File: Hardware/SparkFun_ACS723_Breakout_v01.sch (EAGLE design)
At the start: 13 parts

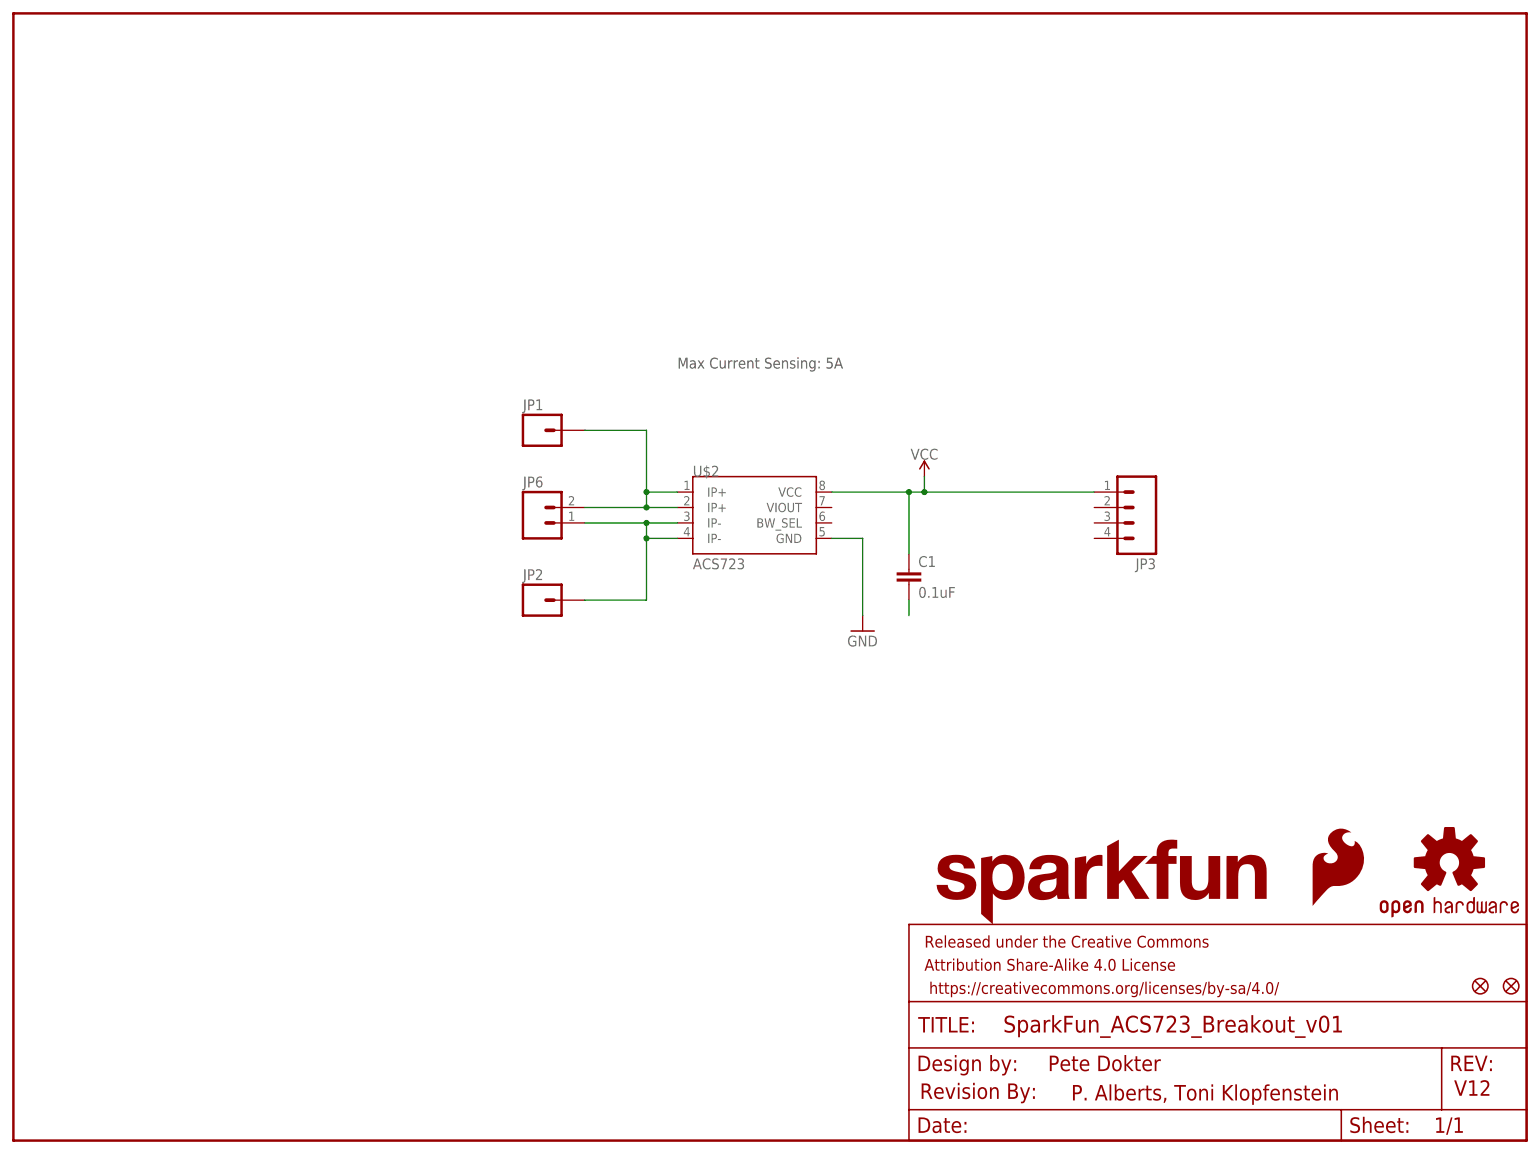
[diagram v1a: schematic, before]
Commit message: Finalizing v01 hardware
-Adjusted silk
-Isolated high current side of the board
-added recommended filter caps
-added band-width select jumper
-changed version number
-changed chip package to ACS723
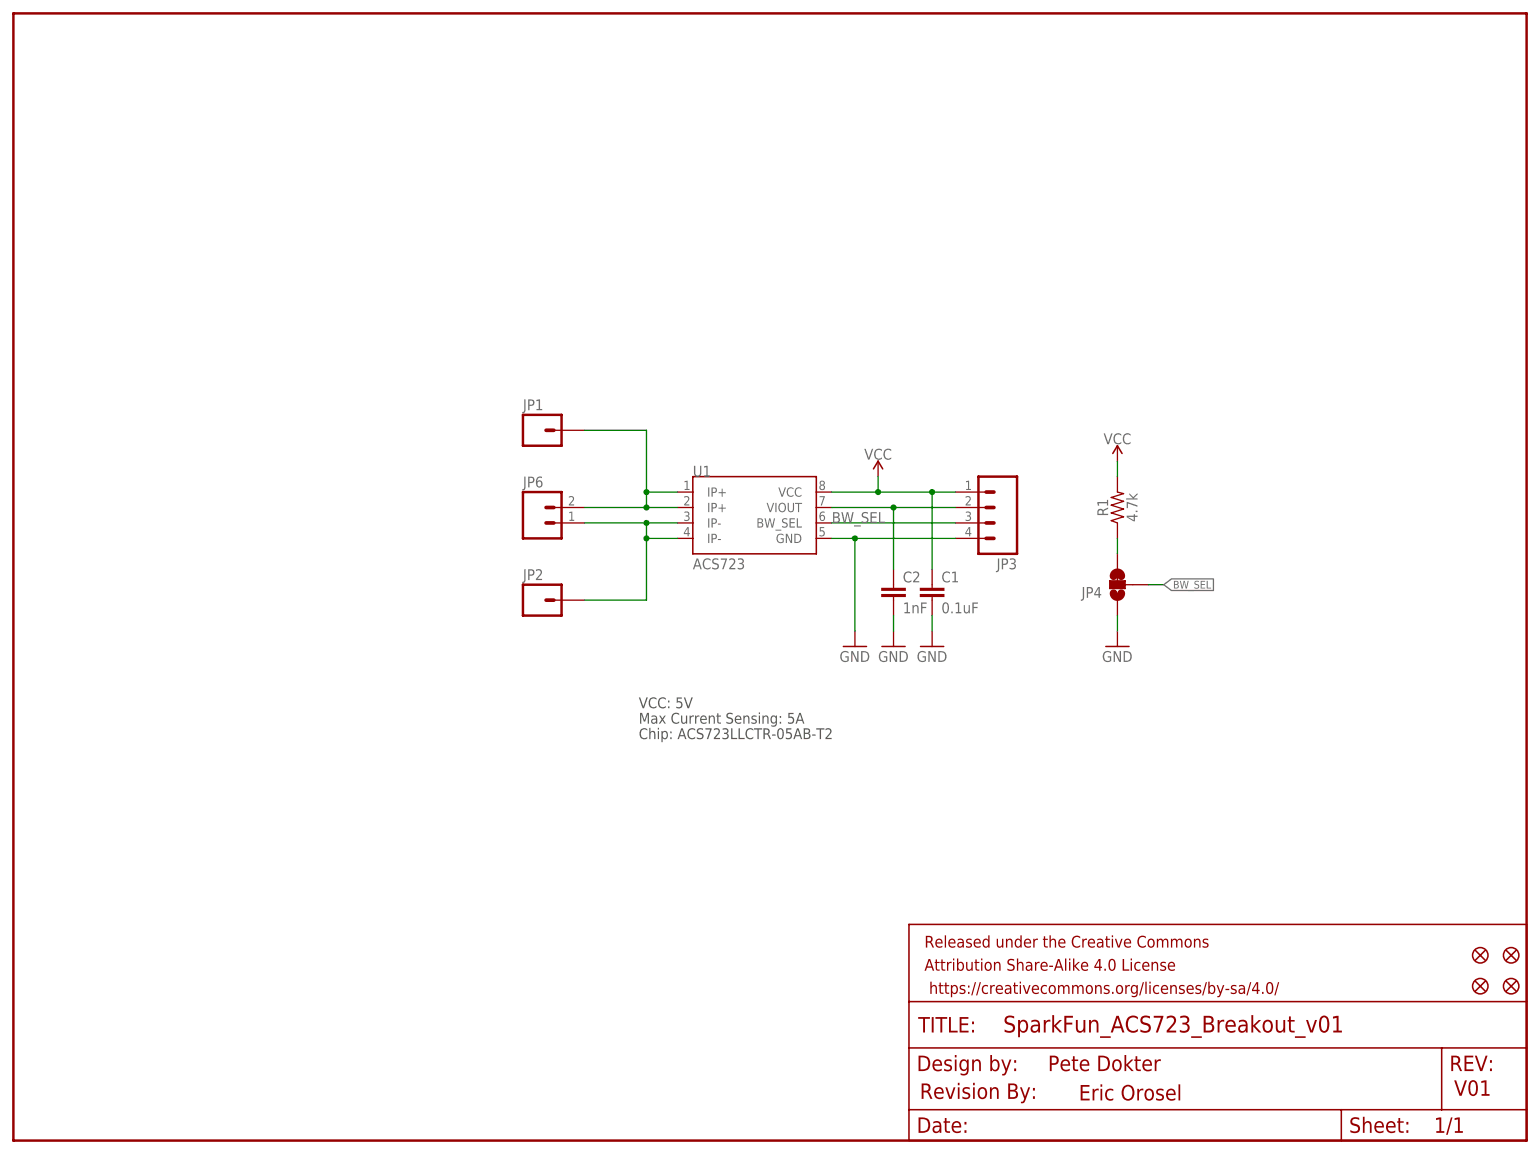
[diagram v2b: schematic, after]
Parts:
- removed JP5: FIDUCIALUFIDUCIAL, SparkFun-Aesthetics:FIDUCIALUFIDUCIAL
- removed LOGO1: SFE_LOGO_NAME.1_INCH, SparkFun-Aesthetics:SFE_LOGO_NAME.1_INCH
- removed LOGO2: SFE_LOGO_FLAME.3_INCH, SparkFun-Aesthetics:SFE_LOGO_FLAME.3_INCH
- removed U$3: OSHW-LOGOS, SparkFun:OSHW-LOGOS
- added C2: 1nF, SparkFun-Capacitors:1.0NF/1000PF-0603-50V-10%
- added FD2, FD3, FD4, FD5: FIDUCIAL1X2, SparkFun-Aesthetics:FIDUCIAL1X2
- added R1: 4.7k, SparkFun-Resistors:4.7KOHM-0603-1/10W-1%
- JP4: value FIDUCIALUFIDUCIAL -> JUMPER-SMT_3_1-NC_TRACE_SILK; device SparkFun-Aesthetics:FIDUCIALUFIDUCIAL -> SparkFun-Jumpers:JUMPER-SMT_3_1-NC_TRACE_SILK
- renumbered U$2 to U1
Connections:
- new net BW_SEL: JP3.3, JP4.2, U1.BW_SEL
- new net GND: C1.2, C2.2, JP3.4, JP4.1, U1.GND
- new net N$3: JP4.3, R1.1
- net N$1: now also C2.1, JP3.2, U1.VIOUT; no longer C1.2
- net VCC: now also R1.2, U1.VCC
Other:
- note added: "Chip: ACS723LLCTR-05AB-T2"
- note added: "Eric Orosel"
- note added: "V01"
- note added: "VCC: 5V"
- note removed: "P. Alberts, Toni Klopfenstein"
- note removed: "V12"
- moved on the sheet: C1, JP3
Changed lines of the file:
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@@
 <part name="JP2" library="SparkFun-Connectors" deviceset="M01" device="-SMTSO-256-ET"/>
 <part name="JP3" library="SparkFun-Connectors" deviceset="M04" device="PTH"/>
-<part name="U$3" library="SparkFun" deviceset="OSHW-LOGO" device="S"/>
-<part name="JP4" library="SparkFun-Aesthetics" deviceset="FIDUCIAL" device="UFIDUCIAL"/>
-<part name="JP5" library="SparkFun-Aesthetics" deviceset="FIDUCIAL" device="UFIDUCIAL"/>
 <part name="JP6" library="SparkFun-Connectors" deviceset="M02" device="1X02_NO_SILK"/>
-<part name="LOGO2" library="SparkFun-Aesthetics" deviceset="SFE_LOGO_FLAME" device=".3_INCH"/>
-<part name="LOGO1" library="SparkFun-Aesthetics" deviceset="SFE_LOGO_NAME" device=".1_INCH"/>
 <part name="SUPPLY1" library="SparkFun-PowerSymbols" deviceset="VCC" device=""/>
 <part name="GND1" library="SparkFun-Aesthetics" deviceset="GND" device=""/>
 <part name="U$1" library="SparkFun-Aesthetics" deviceset="REVISION" device=""/>
-<part name="U$2" library="SparkFun-IC-Power" deviceset="ACS723" device=""/>
+<part name="U1" library="SparkFun-IC-Power" deviceset="ACS723" device=""/>
 <part name="C1" library="SparkFun-Capacitors" deviceset="0.1UF" device="-0603-25V-(+80/-20%)" value="0.1uF"/>
+<part name="GND2" library="SparkFun-Aesthetics" deviceset="GND" device=""/>
+<part name="FD2" library="SparkFun-Aesthetics" deviceset="FIDUCIAL" device="1X2"/>
+<part name="FD3" library="SparkFun-Aesthetics" deviceset="FIDUCIAL" device="1X2"/>
+<part name="FD4" library="SparkFun-Aesthetics" deviceset="FIDUCIAL" device="1X2"/>
+<part name="FD5" library="SparkFun-Aesthetics" deviceset="FIDUCIAL" device="1X2"/>
+<part name="JP4" library="SparkFun-Jumpers" deviceset="JUMPER-SMT_3_1-NC_TRACE" device="_SILK"/>
+<part name="GND4" library="SparkFun-Aesthetics" deviceset="GND" device=""/>
+<part name="R1" library="SparkFun-Resistors" deviceset="4.7KOHM" device="-0603-1/10W-1%" value="4.7k"/>
+<part name="SUPPLY2" library="SparkFun-PowerSymbols" deviceset="VCC" device=""/>
+<part name="C2" library="SparkFun-Capacitors" deviceset="1.0NF/1000PF" device="-0603-50V-10%" value="1nF"/>
+<part name="GND3" library="SparkFun-Aesthetics" deviceset="GND" device=""/>
 </parts>
 <sheets>
@@
 <plain>
 <text x="170.18" y="11.43" size="2.54" layer="94">Pete Dokter</text>
-<text x="236.982" y="7.366" size="2.54" layer="94">V12</text>
-<text x="173.99" y="6.604" size="2.54" layer="94">P. Alberts, Toni Klopfenstein</text>
-<text x="109.22" y="127" size="1.778" layer="97">Max Current Sensing: 5A</text>
+<text x="236.982" y="7.366" size="2.54" layer="94">V01</text>
+<text x="175.26" y="6.604" size="2.54" layer="94">Eric Orosel</text>
+<text x="102.87" y="68.58" size="1.778" layer="97">Max Current Sensing: 5A</text>
+<text x="102.87" y="71.12" size="1.778" layer="97">VCC: 5V</text>
+<text x="102.87" y="66.04" size="1.778" layer="97">Chip: ACS723LLCTR-05AB-T2</text>
 </plain>
 <instances>
@@
 <instance part="JP1" gate="G$1" x="86.36" y="116.84"/>
 <instance part="JP2" gate="G$1" x="86.36" y="88.9"/>
-<instance part="JP3" gate="G$1" x="182.88" y="104.14" rot="R180"/>
-<instance part="U$3" gate="G$1" x="236.22" y="45.72"/>
-<instance part="JP4" gate="G$1" x="246.38" y="25.4"/>
-<instance part="JP5" gate="G$1" x="241.3" y="25.4"/>
+<instance part="JP3" gate="G$1" x="160.02" y="104.14" rot="R180"/>
 <instance part="JP6" gate="G$1" x="86.36" y="101.6"/>
-<instance part="LOGO2" gate="G$1" x="213.36" y="38.1"/>
-<instance part="LOGO1" gate="G$1" x="149.86" y="35.56"/>
-<instance part="SUPPLY1" gate="G$1" x="149.86" y="109.22"/>
-<instance part="GND1" gate="1" x="139.7" y="83.82"/>
+<instance part="SUPPLY1" gate="G$1" x="142.24" y="109.22"/>
+<instance part="GND1" gate="1" x="138.43" y="81.28"/>
 <instance part="U$1" gate="G$1" x="149.098" y="6.858"/>
-<instance part="U$2" gate="G$1" x="121.92" y="101.6"/>
-<instance part="C1" gate="G$1" x="147.32" y="91.44"/>
+<instance part="U1" gate="G$1" x="121.92" y="101.6"/>
+<instance part="C1" gate="G$1" x="151.13" y="88.9"/>
+<instance part="GND2" gate="1" x="151.13" y="81.28"/>
+<instance part="FD2" gate="G$1" x="246.38" y="30.48"/>
+<instance part="FD3" gate="G$1" x="241.3" y="30.48"/>
+<instance part="FD4" gate="G$1" x="241.3" y="25.4"/>
+<instance part="FD5" gate="G$1" x="246.38" y="25.4"/>
+<instance part="JP4" gate="G$1" x="181.61" y="91.44" smashed="yes" rot="R180">
+<attribute name="NAME" x="179.07" y="91.059" size="1.778" layer="95" font="vector" rot="R180"/>
+</instance>
+<instance part="GND4" gate="1" x="181.61" y="81.28"/>
+<instance part="R1" gate="G$1" x="181.61" y="104.14" rot="R90"/>
+<instance part="SUPPLY2" gate="G$1" x="181.61" y="111.76"/>
+<instance part="C2" gate="G$1" x="144.78" y="88.9"/>
+<instance part="GND3" gate="1" x="144.78" y="81.28"/>
 </instances>
 <busses>
@@
 <wire x1="93.98" y1="104.14" x2="104.14" y2="104.14" width="0.1524" layer="91"/>
 <junction x="104.14" y="104.14"/>
-<pinref part="U$2" gate="G$1" pin="IP+@1"/>
-<pinref part="U$2" gate="G$1" pin="IP+@2"/>
+<pinref part="U1" gate="G$1" pin="IP+@1"/>
+<pinref part="U1" gate="G$1" pin="IP+@2"/>
 </segment>
 </net>
@@
 <wire x1="93.98" y1="101.6" x2="104.14" y2="101.6" width="0.1524" layer="91"/>
 <junction x="104.14" y="101.6"/>
-<pinref part="U$2" gate="G$1" pin="IP-@2"/>
-<pinref part="U$2" gate="G$1" pin="IP-@1"/>
+<pinref part="U1" gate="G$1" pin="IP-@2"/>
+<pinref part="U1" gate="G$1" pin="IP-@1"/>
 </segment>
 </net>
-<net name="VCC" class="0">
+<net name="VCC" class="3">
 <segment>
-<wire x1="134.62" y1="106.68" x2="147.32" y2="106.68" width="0.1524" layer="91"/>
-<wire x1="147.32" y1="106.68" x2="149.86" y2="106.68" width="0.1524" layer="91"/>
-<wire x1="149.86" y1="106.68" x2="149.86" y2="109.22" width="0.1524" layer="91"/>
+<wire x1="142.24" y1="106.68" x2="142.24" y2="109.22" width="0.1524" layer="91"/>
 <pinref part="SUPPLY1" gate="G$1" pin="VCC"/>
 <pinref part="C1" gate="G$1" pin="1"/>
-<wire x1="147.32" y1="96.52" x2="147.32" y2="106.68" width="0.1524" layer="91"/>
-<junction x="147.32" y="106.68"/>
+<wire x1="151.13" y1="93.98" x2="151.13" y2="106.68" width="0.1524" layer="91"/>
 <pinref part="JP3" gate="G$1" pin="1"/>
-<wire x1="149.86" y1="106.68" x2="177.8" y2="106.68" width="0.1524" layer="91"/>
-<junction x="149.86" y="106.68"/>
+<junction x="142.24" y="106.68"/>
+<pinref part="U1" gate="G$1" pin="VCC"/>
+<wire x1="151.13" y1="106.68" x2="154.94" y2="106.68" width="0.1524" layer="91"/>
+<wire x1="134.62" y1="106.68" x2="142.24" y2="106.68" width="0.1524" layer="91"/>
+<junction x="151.13" y="106.68"/>
+<wire x1="142.24" y1="106.68" x2="151.13" y2="106.68" width="0.1524" layer="91"/>
+</segment>
+<segment>
+<pinref part="R1" gate="G$1" pin="2"/>
+<wire x1="181.61" y1="109.22" x2="181.61" y2="111.76" width="0.1524" layer="91"/>
+<pinref part="SUPPLY2" gate="G$1" pin="VCC"/>
 </segment>
 </net>
-<net name="GND" class="0">
+<net name="GND" class="3">
 <segment>
-<wire x1="134.62" y1="99.06" x2="139.7" y2="99.06" width="0.1524" layer="91"/>
-<wire x1="139.7" y1="99.06" x2="139.7" y2="86.36" width="0.1524" layer="91"/>
+<wire x1="138.43" y1="99.06" x2="138.43" y2="83.82" width="0.1524" layer="91"/>
 <pinref part="GND1" gate="1" pin="GND"/>
+<pinref part="JP3" gate="G$1" pin="4"/>
+<wire x1="138.43" y1="99.06" x2="154.94" y2="99.06" width="0.1524" layer="91"/>
+<pinref part="U1" gate="G$1" pin="GND"/>
+<wire x1="138.43" y1="99.06" x2="134.62" y2="99.06" width="0.1524" layer="91"/>
+<junction x="138.43" y="99.06"/>
+</segment>
+<segment>
+<pinref part="C1" gate="G$1" pin="2"/>
+<wire x1="151.13" y1="86.36" x2="151.13" y2="83.82" width="0.1524" layer="91"/>
+<pinref part="GND2" gate="1" pin="GND"/>
+</segment>
+<segment>
+<pinref part="JP4" gate="G$1" pin="1"/>
+<wire x1="181.61" y1="86.36" x2="181.61" y2="83.82" width="0.1524" layer="91"/>
+<pinref part="GND4" gate="1" pin="GND"/>
+</segment>
+<segment>
+<pinref part="C2" gate="G$1" pin="2"/>
+<wire x1="144.78" y1="86.36" x2="144.78" y2="83.82" width="0.1524" layer="91"/>
+<pinref part="GND3" gate="1" pin="GND"/>
 </segment>
 </net>
-<net name="N$1" class="7">
+<net name="N$1" class="3">
 <segment>
-<pinref part="C1" gate="G$1" pin="2"/>
-<wire x1="147.32" y1="88.9" x2="147.32" y2="86.36" width="0.1524" layer="91"/>
+<pinref part="U1" gate="G$1" pin="VIOUT"/>
+<pinref part="JP3" gate="G$1" pin="2"/>
+<wire x1="134.62" y1="104.14" x2="144.78" y2="104.14" width="0.1524" layer="91"/>
+<wire x1="144.78" y1="104.14" x2="154.94" y2="104.14" width="0.1524" layer="91"/>
+<wire x1="144.78" y1="104.14" x2="144.78" y2="93.98" width="0.1524" layer="91"/>
+<junction x="144.78" y="104.14"/>
+<pinref part="C2" gate="G$1" pin="1"/>
 </segment>
 </net>
+<net name="BW_SEL" class="3">
+<segment>
+<pinref part="U1" gate="G$1" pin="BW_SEL"/>
+<pinref part="JP3" gate="G$1" pin="3"/>
+<wire x1="134.62" y1="101.6" x2="154.94" y2="101.6" width="0.1524" layer="91"/>
+<label x="134.62" y="101.6" size="1.778" layer="95"/>
+</segment>
+<segment>
+<pinref part="JP4" gate="G$1" pin="2"/>
+<wire x1="186.69" y1="91.44" x2="189.23" y2="91.44" width="0.1524" layer="91"/>
+<label x="189.23" y="91.44" size="1.27" layer="95" xref="yes"/>
+</segment>
+</net>
+<net name="N$3" class="3">
+<segment>
+<pinref part="JP4" gate="G$1" pin="3"/>
+<wire x1="181.61" y1="96.52" x2="181.61" y2="99.06" width="0.1524" layer="91"/>
+<pinref part="R1" gate="G$1" pin="1"/>
+</segment>
+</net>

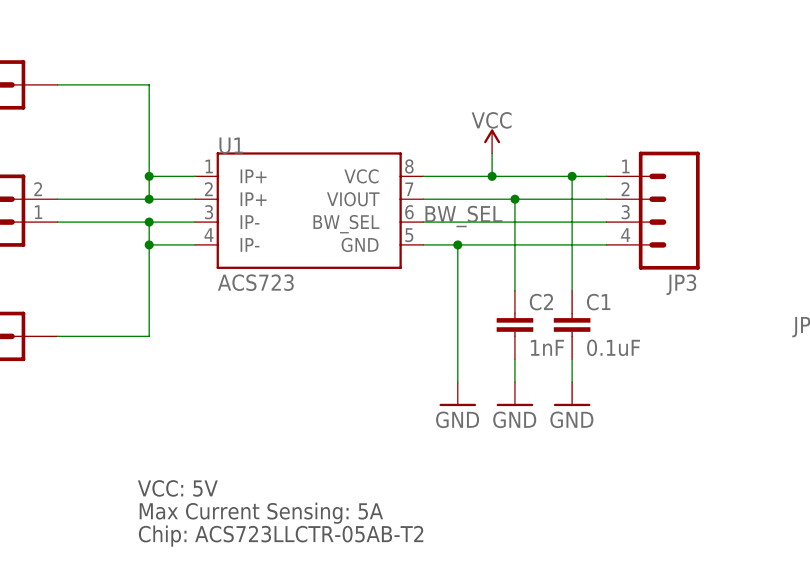
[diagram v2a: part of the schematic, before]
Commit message: Added designer attributes
-Added "designed by" and "Revised by" attributes and frame
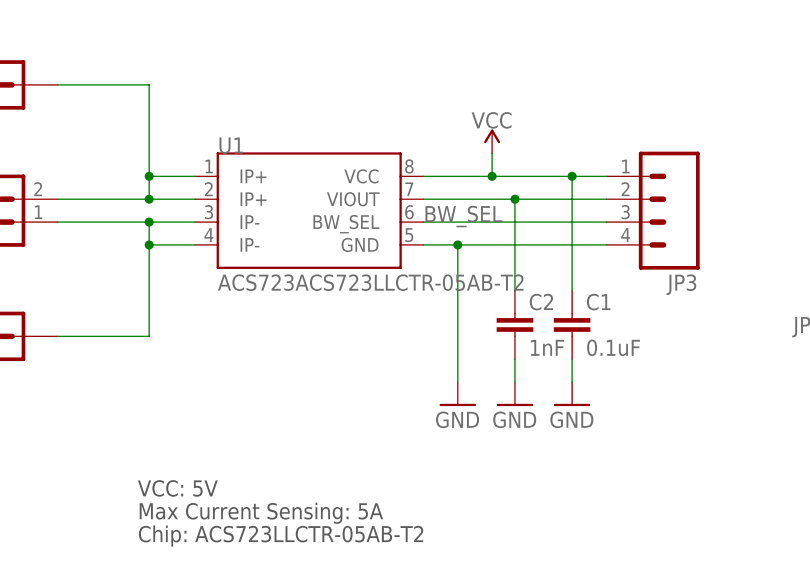
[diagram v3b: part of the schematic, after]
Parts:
- FRAME1: value (none) -> FRAME-LETTER
- U1: value ACS723 -> ACS723ACS723LLCTR-05AB-T2; device SparkFun-IC-Power:ACS723 -> SparkFun-IC-Power:ACS723ACS723LLCTR-05AB-T2
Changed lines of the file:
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@@
 </classes>
 <parts>
-<part name="FRAME1" library="SparkFun-Aesthetics" deviceset="FRAME-LETTER" device=""/>
 <part name="JP1" library="SparkFun-Connectors" deviceset="M01" device="-SMTSO-256-ET"/>
 <part name="JP2" library="SparkFun-Connectors" deviceset="M01" device="-SMTSO-256-ET"/>
@@
 <part name="GND1" library="SparkFun-Aesthetics" deviceset="GND" device=""/>
 <part name="U$1" library="SparkFun-Aesthetics" deviceset="REVISION" device=""/>
-<part name="U1" library="SparkFun-IC-Power" deviceset="ACS723" device=""/>
+<part name="U1" library="SparkFun-IC-Power" deviceset="ACS723" device="" technology="ACS723LLCTR-05AB-T2"/>
 <part name="C1" library="SparkFun-Capacitors" deviceset="0.1UF" device="-0603-25V-(+80/-20%)" value="0.1uF"/>
 <part name="GND2" library="SparkFun-Aesthetics" deviceset="GND" device=""/>
@@
 <part name="C2" library="SparkFun-Capacitors" deviceset="1.0NF/1000PF" device="-0603-50V-10%" value="1nF"/>
 <part name="GND3" library="SparkFun-Aesthetics" deviceset="GND" device=""/>
+<part name="FRAME1" library="SparkFun-Aesthetics" deviceset="FRAME-LETTER" device=""/>
 </parts>
 <sheets>
@@
 </plain>
 <instances>
-<instance part="FRAME1" gate="G$1" x="0" y="0"/>
-<instance part="FRAME1" gate="V" x="147.32" y="0"/>
 <instance part="JP1" gate="G$1" x="86.36" y="116.84"/>
 <instance part="JP2" gate="G$1" x="86.36" y="88.9"/>
@@
 <instance part="C2" gate="G$1" x="144.78" y="88.9"/>
 <instance part="GND3" gate="1" x="144.78" y="81.28"/>
+<instance part="FRAME1" gate="G$1" x="0" y="0"/>
+<instance part="FRAME1" gate="V" x="147.32" y="0"/>
 </instances>
 <busses>
